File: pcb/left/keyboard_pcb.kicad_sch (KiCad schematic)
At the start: 105 parts, among them J3 Alt. Battery, J4 Conn_01x01_Socket, K00 KEYSW, K01 KEYSW, K02 KEYSW, K03 KEYSW, K04 KEYSW, K05 KEYSW, K10 KEYSW, K11 KEYSW, K12 KEYSW, K13 KEYSW, K14 KEYSW, K15 KEYSW, K20 KEYSW, K21 KEYSW, K22 KEYSW, K23 KEYSW, K24 KEYSW, K25 KEYSW, K33 KEYSW, K34 KEYSW, K35 KEYSW, U1 Flippable RP2040 ProMicro/nic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

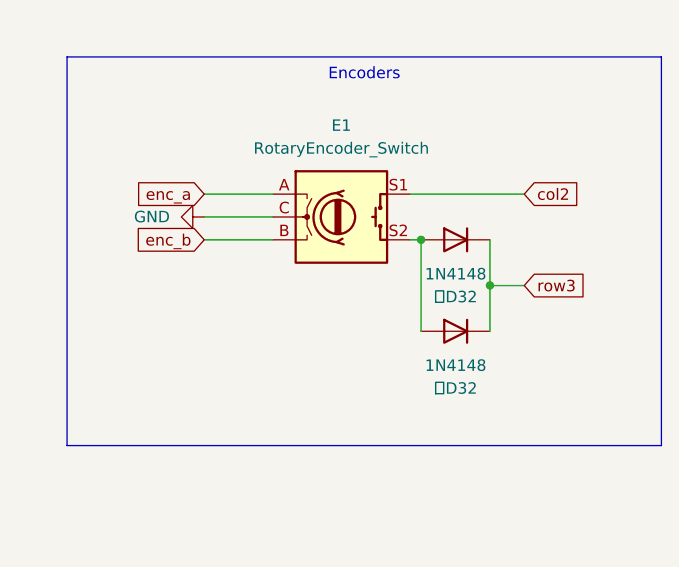
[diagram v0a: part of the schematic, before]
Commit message: Connect encoder to MCU, separate left and right side encoder switch to diode connection
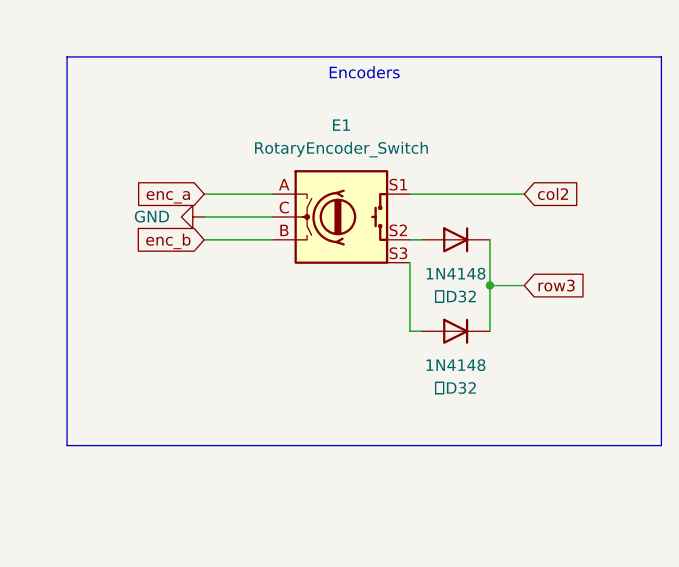
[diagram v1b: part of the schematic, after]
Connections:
- net at E1.S2, 左D32.2 (A): no longer 右D32.2 (A)
- new net: E1.S3, 右D32.2 (A)
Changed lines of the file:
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@@
   (junction (at 259.08 116.84) (diameter 0) (color 0 0 0 0)
   )
-  (junction (at 313.6561 205.74) (diameter 0) (color 0 0 0 0)
-  )
   (junction (at 226.06 220.98) (diameter 0) (color 0 0 0 0)
   )
@@
     (stroke (width 0) (type default))
   )
-  (wire (pts (xy 313.6561 205.74) (xy 313.6561 215.9))
-    (stroke (width 0) (type default))
-  )
   (wire (pts (xy 332.74 109.22) (xy 332.74 127))
     (stroke (width 0) (type default))
@@
     (stroke (width 0) (type default))
   )
-  (wire (pts (xy 313.69 205.74) (xy 313.6561 205.74))
+  (wire (pts (xy 312.42 205.74) (xy 313.69 205.74))
     (stroke (width 0) (type default))
   )
@@
     (stroke (width 0) (type default))
   )
+  (wire (pts (xy 312.42 215.9) (xy 313.69 215.9))
+    (stroke (width 0) (type default))
+  )
   (wire (pts (xy 91.44 53.34) (xy 86.36 53.34))
     (stroke (width 0) (type default))
@@
     (stroke (width 0) (type default))
   )
-  (wire (pts (xy 313.6561 205.74) (xy 312.42 205.74))
-    (stroke (width 0) (type default))
-  )
   (wire (pts (xy 88.9 40.64) (xy 86.36 40.64))
     (stroke (width 0) (type default))
@@
     (stroke (width 0) (type default))
   )
+  (wire (pts (xy 312.42 208.28) (xy 312.42 215.9))
+    (stroke (width 0) (type default))
+  )
   (wire (pts (xy 332.74 101.6) (xy 332.74 109.22))
     (stroke (width 0) (type default))
@@
     (stroke (width 0) (type default))
   )
-  (wire (pts (xy 313.69 215.9) (xy 313.6561 215.9))
-    (stroke (width 0) (type default))
-  )
   (wire (pts (xy 193.04 144.78) (xy 198.12 144.78))
     (stroke (width 0) (type default))
@@
     (pin "A")
     (pin "C")
+    (pin "S3")
     (instances
       (project "keyboard_pcb"

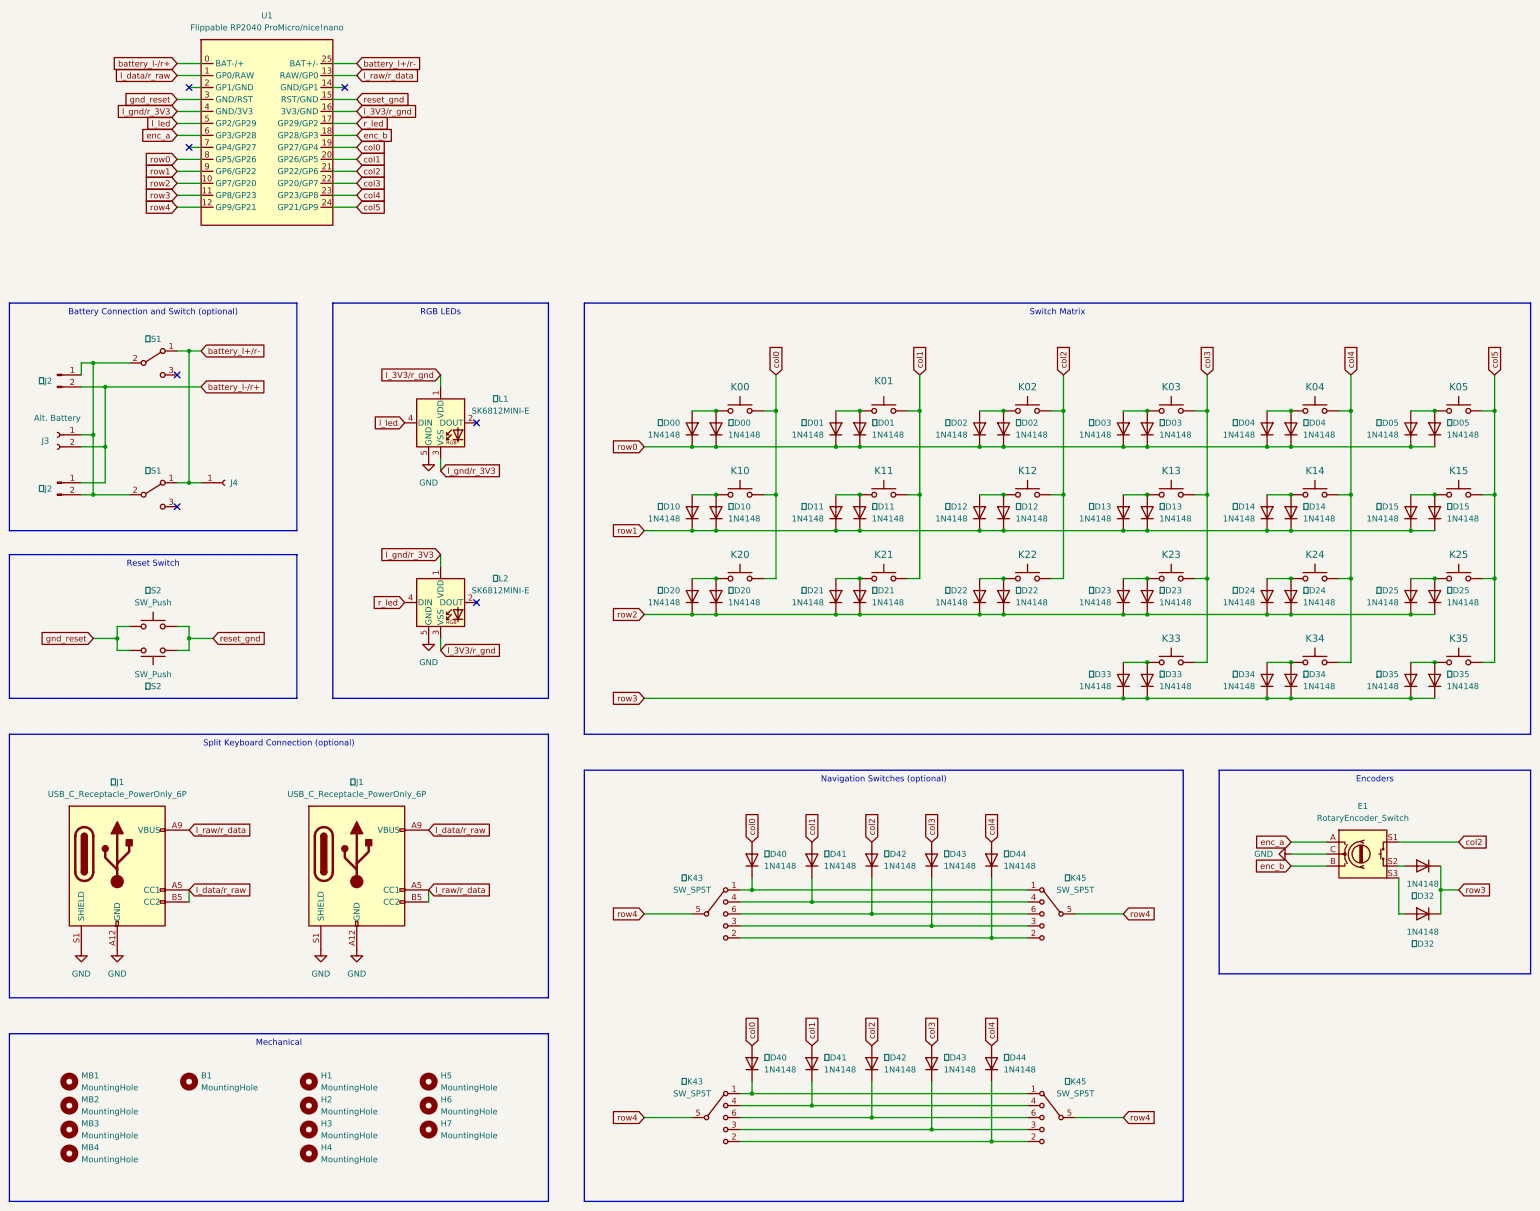
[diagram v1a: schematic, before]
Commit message: Add tracks connecting rows and columns to MCU, swap LED and Encoder pins for ease of routing
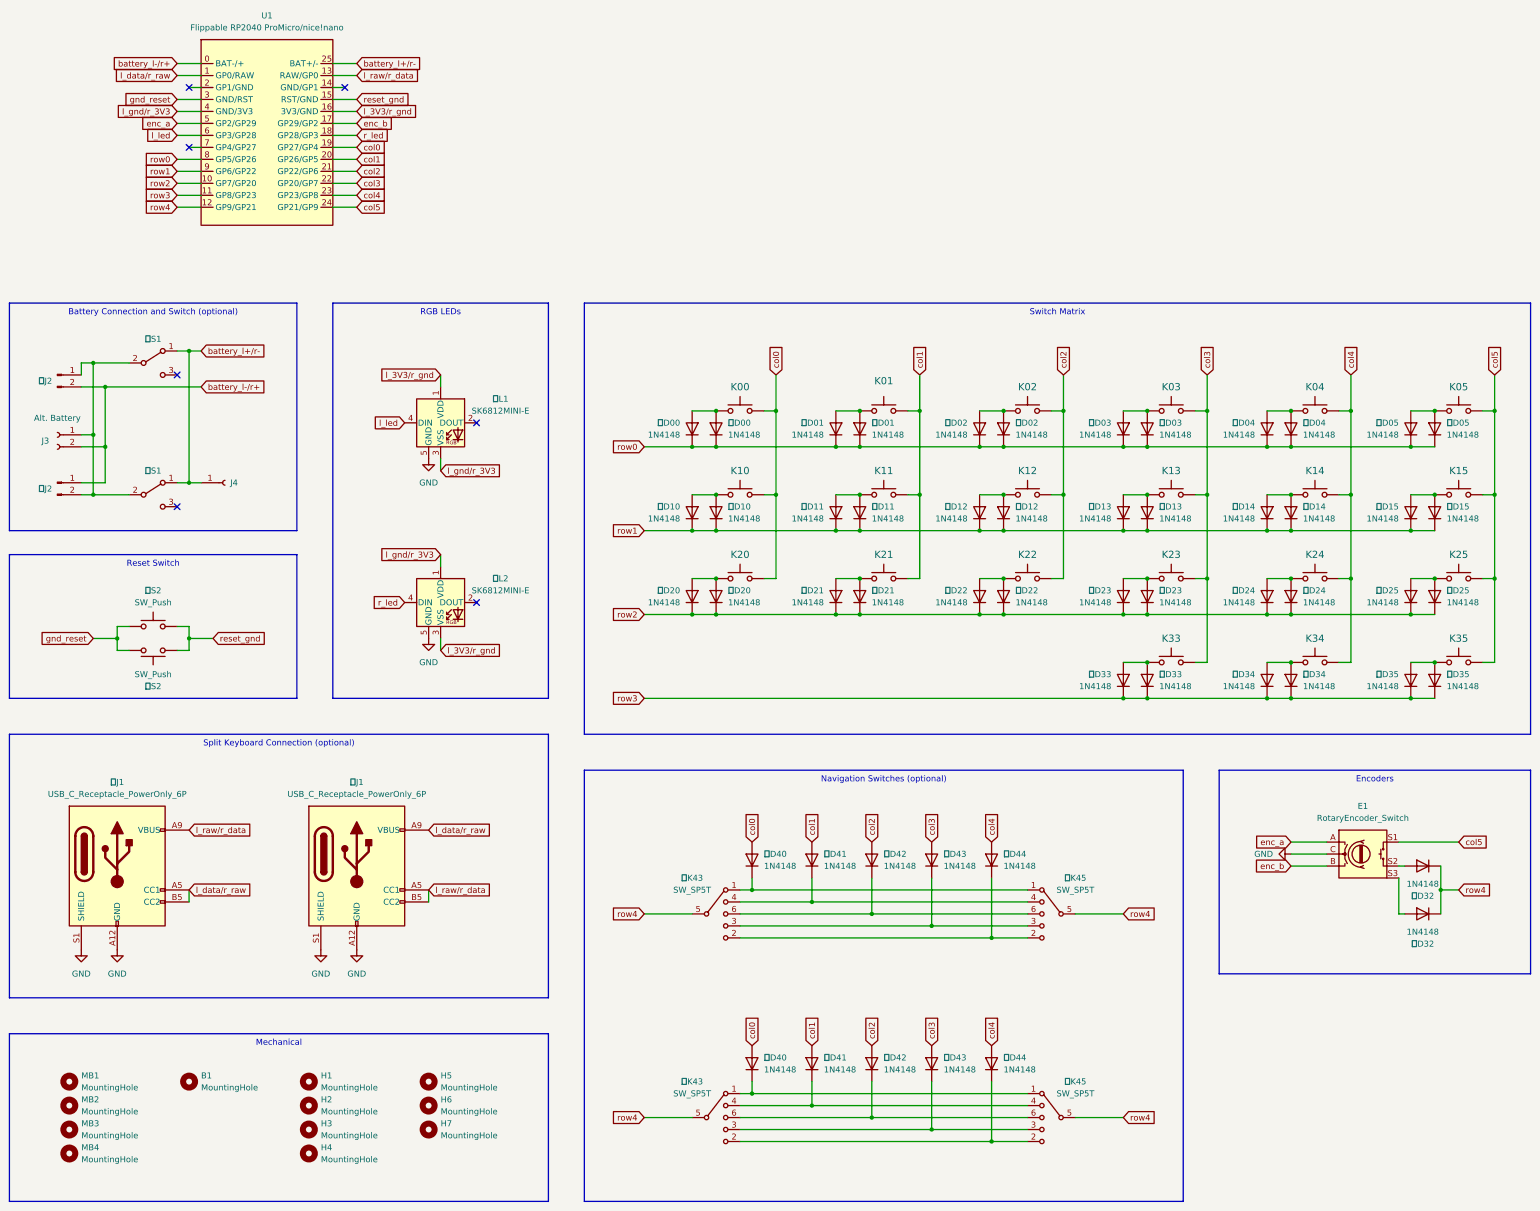
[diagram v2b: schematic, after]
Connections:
- net col2: no longer E1.S1
- net col5: now also E1.S1
- net enc_a: now also U1.5 (GP2/GP29); no longer U1.6 (GP3/GP28)
- net enc_b: now also U1.17 (GP29/GP2); no longer U1.18 (GP28/GP3)
- net l_led: now also U1.6 (GP3/GP28); no longer U1.5 (GP2/GP29)
- net r_led: now also U1.18 (GP28/GP3); no longer U1.17 (GP29/GP2)
- net row3: no longer 右D32.1 (K), 左D32.1 (K)
- net row4: now also 右D32.1 (K), 左D32.1 (K)
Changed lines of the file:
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@@
+    )
+  )
+  (global_label "enc_b" (shape input) (at 91.44 48.26 0) (fields_autoplaced)
+    (effects (font (size 1.27 1.27)) (justify left))
+    (property "Intersheetrefs" "${INTERSHEET_REFS}" (at 99.868 48.26 0)
+      (effects (font (size 1.27 1.27)) (justify left) hide)
     )
   )
@@
     )
   )
-  (global_label "l_led" (shape input) (at 53.34 48.26 180) (fields_autoplaced)
-    (effects (font (size 1.27 1.27)) (justify right))
-    (property "Intersheetrefs" "${INTERSHEET_REFS}" (at 43.2792 48.26 0)
-      (effects (font (size 1.27 1.27)) (justify right) hide)
-    )
-  )
   (global_label "row4" (shape input) (at 152.4 259.08 180) (fields_autoplaced)
     (effects (font (size 1.27 1.27)) (justify right))
@@
     )
   )
+  (global_label "enc_a" (shape input) (at 53.34 48.26 180) (fields_autoplaced)
+    (effects (font (size 1.27 1.27)) (justify right))
+    (property "Intersheetrefs" "${INTERSHEET_REFS}" (at 44.912 48.26 0)
+      (effects (font (size 1.27 1.27)) (justify right) hide)
+    )
+  )
   (global_label "l_raw{slash}r_data" (shape input) (at 91.44 38.1 0) (fields_autoplaced)
     (effects (font (size 1.27 1.27)) (justify left))
@@
     )
   )
-  (global_label "enc_a" (shape input) (at 53.34 50.8 180) (fields_autoplaced)
-    (effects (font (size 1.27 1.27)) (justify right))
-    (property "Intersheetrefs" "${INTERSHEET_REFS}" (at 44.912 50.8 0)
-      (effects (font (size 1.27 1.27)) (justify right) hide)
-    )
-  )
   (global_label "l_gnd{slash}r_3V3" (shape input) (at 109.22 139.7 180) (fields_autoplaced)
     (effects (font (size 1.27 1.27)) (justify right))
@@
     )
   )
-  (global_label "r_led" (shape input) (at 91.44 48.26 0) (fields_autoplaced)
-    (effects (font (size 1.27 1.27)) (justify left))
-    (property "Intersheetrefs" "${INTERSHEET_REFS}" (at 102.7103 48.26 0)
-      (effects (font (size 1.27 1.27)) (justify left) hide)
-    )
-  )
-  (global_label "row3" (shape input) (at 325.12 210.82 0) (fields_autoplaced)
+  (global_label "row4" (shape input) (at 325.12 210.82 0) (fields_autoplaced)
     (effects (font (size 1.27 1.27)) (justify left))
     (property "Intersheetrefs" "${INTERSHEET_REFS}" (at 332.5804 210.82 0)
@@
     )
   )
+  (global_label "r_led" (shape input) (at 91.44 50.8 0) (fields_autoplaced)
+    (effects (font (size 1.27 1.27)) (justify left))
+    (property "Intersheetrefs" "${INTERSHEET_REFS}" (at 102.7103 50.8 0)
+      (effects (font (size 1.27 1.27)) (justify left) hide)
+    )
+  )
   (global_label "col4" (shape input) (at 302.26 101.6 90) (fields_autoplaced)
     (effects (font (size 1.27 1.27)) (justify left))
@@
     )
   )
-  (global_label "enc_b" (shape input) (at 91.44 50.8 0) (fields_autoplaced)
-    (effects (font (size 1.27 1.27)) (justify left))
-    (property "Intersheetrefs" "${INTERSHEET_REFS}" (at 99.868 50.8 0)
-      (effects (font (size 1.27 1.27)) (justify left) hide)
+  (global_label "l_led" (shape input) (at 53.34 50.8 180) (fields_autoplaced)
+    (effects (font (size 1.27 1.27)) (justify right))
+    (property "Intersheetrefs" "${INTERSHEET_REFS}" (at 43.2792 50.8 0)
+      (effects (font (size 1.27 1.27)) (justify right) hide)
     )
   )
@@
     )
   )
-  (global_label "col2" (shape input) (at 325.12 200.66 0) (fields_autoplaced)
+  (global_label "col5" (shape input) (at 325.12 200.66 0) (fields_autoplaced)
     (effects (font (size 1.27 1.27)) (justify left))
     (property "Intersheetrefs" "${INTERSHEET_REFS}" (at 332.2175 200.66 0)
